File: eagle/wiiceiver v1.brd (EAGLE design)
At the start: 100 x 80 mm, 15 parts, among them IC1 ATmega328P, IC2 317T

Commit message: ordered!
“final” version, ordered from OshPark
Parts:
- added C3: 0.1pF, capacitor-wima:C5B2.5
- CLK: device pinhead:1X03 -> crystal:HC49U
- IC1: device ic-package:DIL28-6 -> ic-package:DIL28-3
- IC2: value 317T -> (none); device linear:TO220H -> v-reg:317TS
- R5, R6, R7, R8: device rcl:0207/7 -> resistor:0204V
- moved C2 36.1 mm to (39.4, 27.9)
- moved IC2 26.9 mm to (50.8, 40.6)
- moved JP4 22.9 mm to (49.5, 62.2)
- moved R7 21.7 mm to (45.7, 62.2), turned to 270 degrees
- moved JP1 20.5 mm to (47.0, 30.5)
- moved JP2 19.3 mm to (52.1, 29.2)
- moved R6 18.5 mm to (45.7, 67.3)
- moved C1 16.7 mm to (49.5, 49.5), turned to 180 degrees
- moved IC1 15.9 mm to (39.4, 49.5)
- moved LED1 15.3 mm to (26.7, 36.8), turned to 270 degrees
- moved LED2 13.1 mm to (26.7, 31.8), turned to 90 degrees
- moved SV1 12.7 mm to (29.2, 62.2)
- moved R8 11.4 mm to (33.0, 67.3), turned to 270 degrees
- moved CLK 9.92 mm to (30.5, 44.5)
- moved R5 7.73 mm to (31.8, 35.6), turned to 0 degrees
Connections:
- removed net N$12: IC1.1, R8.1, SV1.5
- new net N$2: IC1.1, R8.2, SV1.5
- net GND: now also C3.2
- net VIN: now also C3.1, R8.1; no longer R8.2
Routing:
- net GND: track 151.0 -> 101.7 mm
- net VIN: track 119.2 -> 99.1 mm
- net N$6: track 14.6 -> 6.35 mm
- net N$21: track 12.7 -> 6.35 mm
- net N$2: track 0.00 -> 6.35 mm
- net N$12: track 6.35 -> 0.00 mm
- net DIP12: track 3.81 -> 8.89 mm
- net N$11: track 10.2 -> 5.38 mm
- net N$22: track 10.2 -> 6.35 mm
- net N$7: track 6.35 -> 9.66 mm
- net N$16: track 25.4 -> 27.9 mm
- net N$10: track 7.41 -> 5.08 mm
- net N$9: track 7.62 -> 5.38 mm
- net N$1: track 5.08 -> 3.81 mm
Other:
- board size 100 x 80 mm -> 35.2 x 50.8 mm
- board text added: "austindavid.com/wiiceiver"

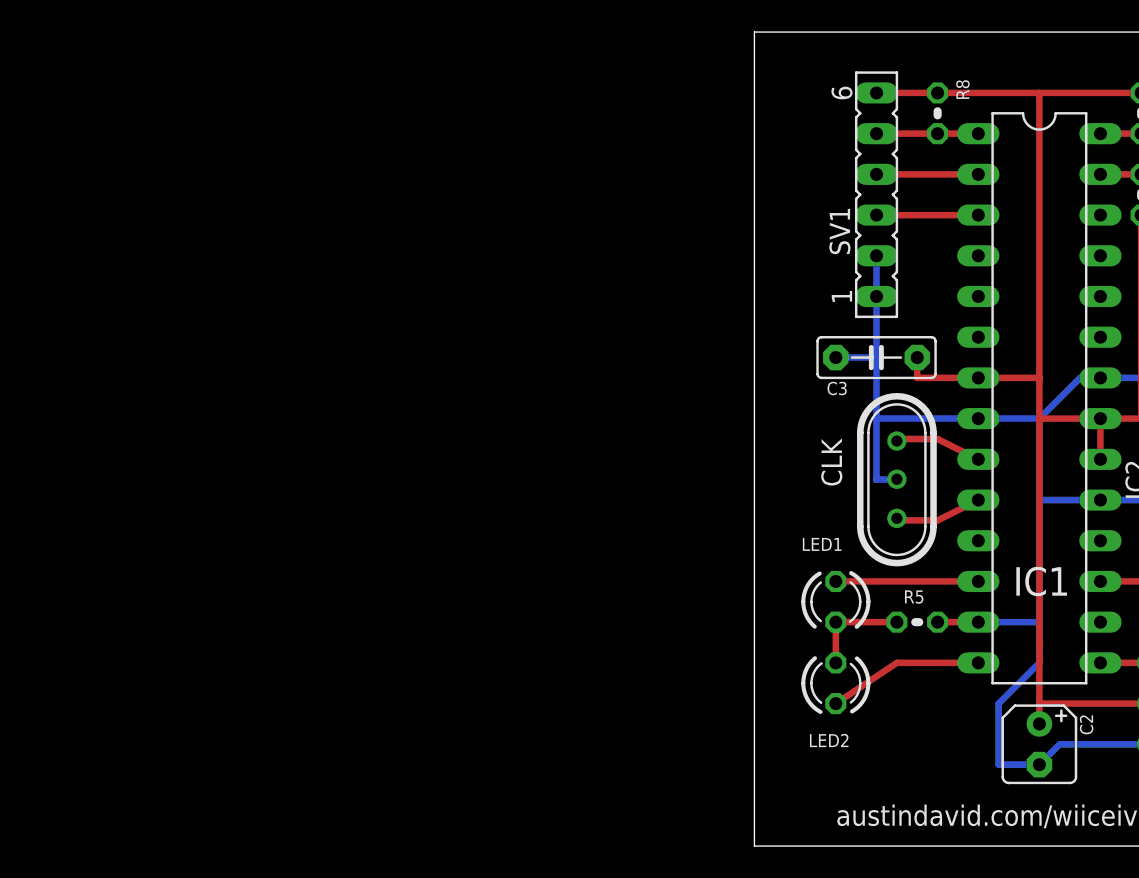
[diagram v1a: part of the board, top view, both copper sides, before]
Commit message: updating PCB slightly
6-pin header was a little tight…
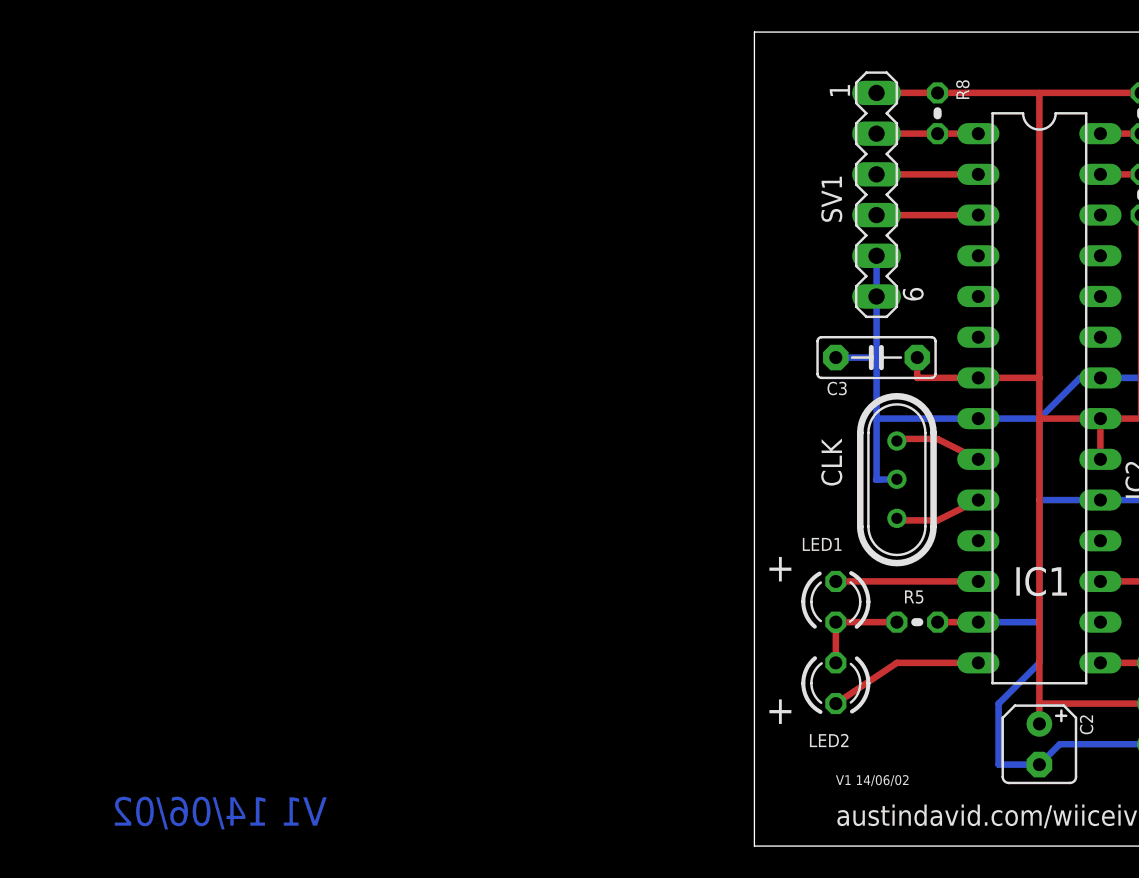
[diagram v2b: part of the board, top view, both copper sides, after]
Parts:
- SV1: value Header -> (none); device con-lsta:FE06 -> con-lstb:MA06-1
- turned SV1 to 270 degrees
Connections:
- net GND: now also SV1.5, SV1.6; no longer SV1.1, SV1.2
- net N$2: now also SV1.2; no longer SV1.5
- net RX: now also SV1.3; no longer SV1.4
- net TX: now also SV1.4; no longer SV1.3
- net VIN: now also SV1.1; no longer SV1.6
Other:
- board text added: "+"
- board text added: "V1 14/06/02"
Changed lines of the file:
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@@
 <wire x1="21.59" y1="72.38" x2="21.59" y2="21.59" width="0" layer="20"/>
 <text x="26.67" y="22.86" size="1.27" layer="25">austindavid.com/wiiceiver</text>
+<text x="24.13" y="29.21" size="1.778" layer="25" rot="MR0">+</text>
+<text x="24.13" y="38.1" size="1.778" layer="25" rot="MR0">+</text>
+<text x="-5.08" y="22.86" size="1.778" layer="16" rot="MR0">V1 14/06/02</text>
+<text x="26.67" y="25.4" size="0.6096" layer="25">V1 14/06/02</text>
 </plain>
 <attributes>
@@
 <attribute name="VALUE" x="30.861" y="28.575" size="1.27" layer="27" ratio="10" rot="R90"/>
 </element>
-<element name="SV1" library="con-lsta" package="FE06" value="Header" x="29.21" y="62.23" rot="R90">
-<attribute name="OC_NEWARK" value="unknown" x="80.01" y="83.82" size="1.778" layer="27" rot="R90" display="off"/>
-<attribute name="MPN" value="" x="80.01" y="83.82" size="1.778" layer="27" rot="R90" display="off"/>
-<attribute name="MF" value="" x="80.01" y="83.82" size="1.778" layer="27" rot="R90" display="off"/>
-<attribute name="OC_FARNELL" value="unknown" x="80.01" y="83.82" size="1.778" layer="27" rot="R90" display="off"/>
-</element>
 <element name="JP1" library="pinhead" package="1X03" value="Servo" x="46.99" y="30.48" rot="R270"/>
 <element name="JP2" library="pinhead" package="1X02" value="BEC" x="52.07" y="29.21" rot="R270"/>
@@
 </element>
 <element name="IC2" library="v-reg" package="317TS" value="" x="50.8" y="40.64" rot="R270"/>
+<element name="SV1" library="con-lstb" package="MA06-1" value="" x="29.21" y="62.23" smashed="yes" rot="R270">
+<attribute name="OC_NEWARK" value="unknown" x="29.21" y="62.23" size="1.778" layer="27" rot="R270" display="off"/>
+<attribute name="MPN" value="" x="29.21" y="62.23" size="1.778" layer="27" rot="R270" display="off"/>
+<attribute name="MF" value="" x="29.21" y="62.23" size="1.778" layer="27" rot="R270" display="off"/>
+<attribute name="OC_FARNELL" value="unknown" x="29.21" y="62.23" size="1.778" layer="27" rot="R270" display="off"/>
+<attribute name="NAME" x="25.781" y="63.5" size="1.27" layer="25" ratio="10" rot="R270"/>
+<attribute name="VALUE" x="26.289" y="64.77" size="1.27" layer="27" ratio="10" rot="R270"/>
+</element>
 </elements>
 <signals>
@@
 </signal>
 <signal name="RX">
-<contactref element="SV1" pad="4"/>
 <contactref element="IC1" pad="2"/>
-<wire x1="29.21" y1="63.5" x2="35.56" y2="63.5" width="0.4064" layer="1"/>
+<contactref element="SV1" pad="3"/>
+<wire x1="35.56" y1="63.5" x2="29.21" y2="63.5" width="0.4064" layer="1"/>
 </signal>
 <signal name="N$10">
@@
 <contactref element="C2" pad="-"/>
 <contactref element="IC1" pad="22"/>
-<contactref element="SV1" pad="1"/>
-<contactref element="SV1" pad="2"/>
 <contactref element="IC1" pad="13"/>
 <contactref element="C1" pad="-"/>
 <contactref element="CLK" pad="2"/>
-<wire x1="29.21" y1="58.42" x2="29.21" y2="55.88" width="0.4064" layer="16"/>
 <wire x1="35.56" y1="35.56" x2="39.37" y2="35.56" width="0.4064" layer="16"/>
 <wire x1="39.37" y1="35.56" x2="39.37" y2="43.18" width="0.4064" layer="16"/>
@@
 <wire x1="52.07" y1="27.94" x2="46.99" y2="27.94" width="0.4064" layer="16"/>
 <wire x1="26.67" y1="52.07" x2="29.21" y2="52.07" width="0.4064" layer="16"/>
-<wire x1="29.21" y1="52.07" x2="29.21" y2="55.88" width="0.4064" layer="16"/>
 <wire x1="29.21" y1="44.45" x2="29.21" y2="48.26" width="0.4064" layer="16"/>
 <wire x1="29.21" y1="48.26" x2="29.21" y2="52.07" width="0.4064" layer="16"/>
@@
 <wire x1="36.83" y1="30.48" x2="36.83" y2="26.67" width="0.4064" layer="16"/>
 <wire x1="36.83" y1="26.67" x2="39.37" y2="26.67" width="0.4064" layer="16"/>
+<contactref element="SV1" pad="6"/>
+<contactref element="SV1" pad="5"/>
+<wire x1="29.21" y1="58.42" x2="29.21" y2="55.88" width="0.4064" layer="16"/>
+<wire x1="29.21" y1="55.88" x2="29.21" y2="52.07" width="0.4064" layer="16"/>
 </signal>
 <signal name="VIN">
@@
 <contactref element="C3" pad="1"/>
 <contactref element="C2" pad="+"/>
-<contactref element="SV1" pad="6"/>
 <contactref element="R7" pad="2"/>
 <contactref element="R6" pad="2"/>
 <contactref element="R8" pad="1"/>
-<wire x1="29.21" y1="68.58" x2="33.02" y2="68.58" width="0.4064" layer="1"/>
 <wire x1="33.02" y1="68.58" x2="39.37" y2="68.58" width="0.4064" layer="1"/>
 <wire x1="39.37" y1="68.58" x2="39.37" y2="50.8" width="0.4064" layer="1"/>
@@
 <wire x1="39.37" y1="30.48" x2="46.99" y2="30.48" width="0.4064" layer="1"/>
 <wire x1="39.37" y1="48.26" x2="43.18" y2="48.26" width="0.4064" layer="1"/>
-<wire x1="39.37" y1="33.02" x2="39.37" y2="34.29" width="0.4064" layer="1"/>
-<wire x1="39.37" y1="34.29" x2="39.37" y2="48.26" width="0.4064" layer="1"/>
+<wire x1="39.37" y1="30.48" x2="39.37" y2="48.26" width="0.4064" layer="1"/>
 <wire x1="39.37" y1="48.26" x2="39.37" y2="50.8" width="0.4064" layer="1"/>
 <wire x1="39.37" y1="29.21" x2="39.37" y2="30.48" width="0.4064" layer="1"/>
-<wire x1="39.37" y1="30.48" x2="39.37" y2="33.02" width="0.4064" layer="1"/>
+<contactref element="SV1" pad="1"/>
+<wire x1="33.02" y1="68.58" x2="29.21" y2="68.58" width="0.4064" layer="1"/>
 </signal>
 <signal name="DIP12">
@@
 <signal name="TX">
 <contactref element="IC1" pad="3"/>
-<contactref element="SV1" pad="3"/>
+<contactref element="SV1" pad="4"/>
 <wire x1="35.56" y1="60.96" x2="29.21" y2="60.96" width="0.4064" layer="1"/>
 </signal>
 <signal name="N$2">
-<contactref element="SV1" pad="5"/>
 <contactref element="IC1" pad="1"/>
 <contactref element="R8" pad="2"/>
-<wire x1="33.02" y1="66.04" x2="29.21" y2="66.04" width="0.4064" layer="1"/>
 <wire x1="33.02" y1="66.04" x2="35.56" y2="66.04" width="0.4064" layer="1"/>
+<contactref element="SV1" pad="2"/>
+<wire x1="29.21" y1="66.04" x2="33.02" y2="66.04" width="0.4064" layer="1"/>
 </signal>
 </signals>
